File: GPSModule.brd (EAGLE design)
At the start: 27.9 x 29.6 mm, 18 parts, among them IC1 MCP1700T-3302E, IC2 FGPMMOPA6H, J1 U.FL-R-SMT-1(10), J2 Interface

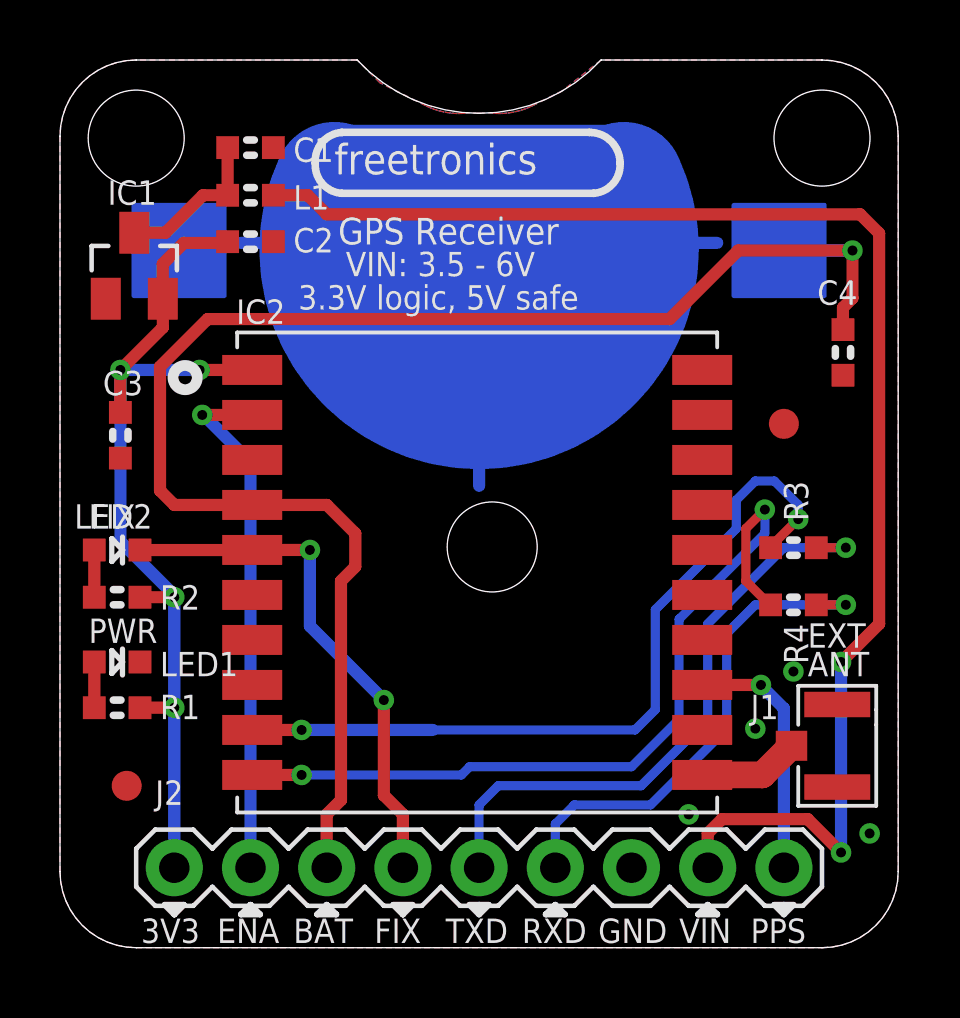
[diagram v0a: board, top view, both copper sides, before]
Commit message: Converted vias to 0.01968504" (0.5mm) drill Added outlines to LEDs Increased label sizes
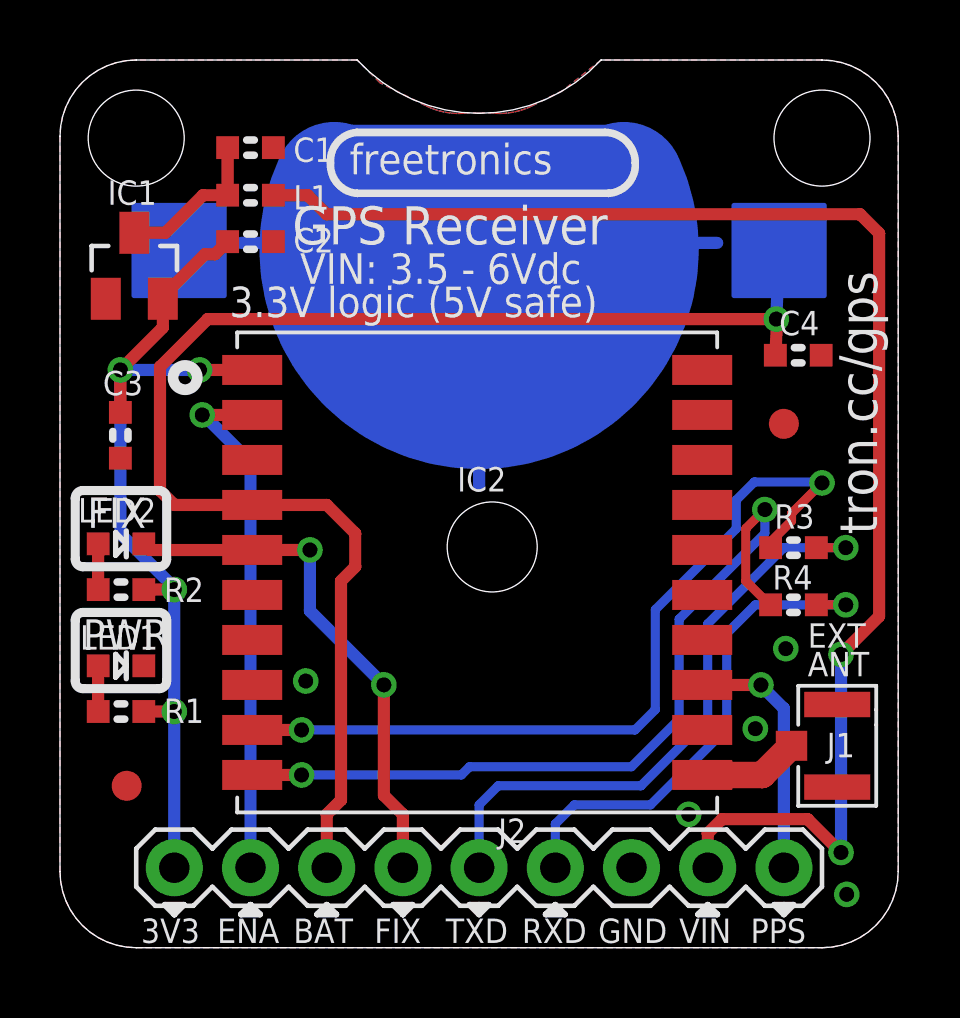
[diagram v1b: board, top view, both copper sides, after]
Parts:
- C1, C4: value 1µF -> 1uF 0603
- C3: value 10nF -> 10nF 0603
- L1: value 600Ω at 100MHz -> 600R at 100MHz
- LED1: value Power -> Power 0603 BLUE
- LED2: value GPS Fix -> GPS Fix 0603 GREEN
- R1: value 1kΩ -> 1K 0603
- R2: value 470Ω -> 470R
- R3, R4: value 0Ω -> 0R 0603
- moved C4 1.50 mm to (24.6, 19.7), turned to 180 degrees
- moved R2 0.28 mm to (2.03, 11.9)
- moved LED2 0.24 mm to (2.03, 13.5)
- moved LED1 0.18 mm to (2.03, 9.40)
- moved R1 0.18 mm to (2.03, 7.87)
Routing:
- net VBAT: track 52.7 -> 47.5 mm
- net TXD: track 26.3 -> 27.8 mm
- net +3V3: track 32.0 -> 31.2 mm
- net GND: vias 4 -> 5
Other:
- board text added: "(C)2014 Freetronics P/L"
- board text added: "3.3V logic (5V safe)"
- board text added: "Default: 9600bps"
- board text added: "Released under the TAPR Open Hardware License: www.tapr.org/OHL"
- board text added: "VIN: 3.5 - 6Vdc"
- board text added: "tron.cc/gps"
- board text removed: "(C)2013 Freetronics"
- board text removed: "3.3V logic, 5V safe"
- board text removed: "VIN: 3.5 - 6V"
- board text removed: "www.freetronics.com/gps"

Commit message: Replaced Greek character with Latin equivalent
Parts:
- C2: value 1µF -> 1uF 0603
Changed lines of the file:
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@@
 <attribute name="VALUE" x="7.77875" y="24.60625" size="0.8128" layer="27" font="vector" ratio="15"/>
 </element>
-<element name="C2" library="freetronics-master-v1" package="0603" value="1µF" x="6.35" y="23.535640625" smashed="yes" rot="R180">
+<element name="C2" library="freetronics-master-v1" package="0603" value="1uF 0603" x="6.35" y="23.535640625" smashed="yes" rot="R180">
 <attribute name="PACKAGE" value="0603" x="6.35" y="23.535640625" size="0.015240625" layer="27" font="vector" rot="R180" display="off"/>
 <attribute name="NAME" x="7.77875" y="23.1775" size="0.8128" layer="25" font="vector" ratio="15"/>
